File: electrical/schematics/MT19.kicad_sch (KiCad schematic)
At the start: 0 parts

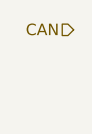
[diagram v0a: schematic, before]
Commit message: Esquematico revisado, agora mais limpo.
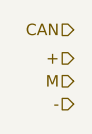
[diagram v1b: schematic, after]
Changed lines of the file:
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@@
 (kicad_sch (version 20211123) (generator eeschema)
   (paper "A4")
+  (hierarchical_label "-" (shape input) (at 48.26 39.37 180)
+    (effects (font (size 1.27 1.27)) (justify right))
+  )
+  (hierarchical_label "+" (shape input) (at 48.26 34.29 180)
+    (effects (font (size 1.27 1.27)) (justify right))
+  )
+  (hierarchical_label "M" (shape input) (at 48.26 36.83 180)
+    (effects (font (size 1.27 1.27)) (justify right))
+  )
   (hierarchical_label "CAN" (shape input) (at 48.26 31.115 180)
     (effects (font (size 1.27 1.27)) (justify right))
